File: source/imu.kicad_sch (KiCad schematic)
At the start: 5 parts

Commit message: Add files via upload
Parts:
- gave numbers to parts that had none: 5
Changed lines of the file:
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@@
   (symbol (lib_id "power:GND") (at 161.29 116.84 0) (unit 1)
     (in_bom yes) (on_board yes)
-    (property "Reference" "#PWR?" (id 0) (at 161.29 123.19 0)
+    (property "Reference" "#PWR0128" (id 0) (at 161.29 123.19 0)
       (effects (font (size 1.27 1.27)) hide)
     )
@@
   (symbol (lib_id "Cheap-FOCer-2-60mm-rescue:BMI160-IMU") (at 146.05 100.33 0) (unit 1)
     (in_bom yes) (on_board yes)
-    (property "Reference" "U?" (id 0) (at 146.05 78.3082 0))
+    (property "Reference" "U2" (id 0) (at 146.05 78.3082 0))
     (property "Value" "BMI160" (id 1) (at 146.05 80.6196 0))
     (property "Footprint" "Package_LGA:Bosch_LGA-14_3x2.5mm_P0.5mm" (id 2) (at 146.05 100.33 0)
@@
   (symbol (lib_id "power:GND") (at 124.46 101.6 0) (unit 1)
     (in_bom yes) (on_board yes)
-    (property "Reference" "#PWR?" (id 0) (at 124.46 107.95 0)
+    (property "Reference" "#PWR0125" (id 0) (at 124.46 107.95 0)
       (effects (font (size 1.27 1.27)) hide)
     )
@@
   (symbol (lib_id "power:VCC") (at 162.56 82.55 0) (unit 1)
     (in_bom yes) (on_board yes)
-    (property "Reference" "#PWR?" (id 0) (at 162.56 86.36 0)
+    (property "Reference" "#PWR0127" (id 0) (at 162.56 86.36 0)
       (effects (font (size 1.27 1.27)) hide)
     )
@@
   (symbol (lib_id "power:GND") (at 179.07 88.9 0) (unit 1)
     (in_bom yes) (on_board yes)
-    (property "Reference" "#PWR?" (id 0) (at 179.07 95.25 0)
+    (property "Reference" "#PWR0129" (id 0) (at 179.07 95.25 0)
       (effects (font (size 1.27 1.27)) hide)
     )
@@
   (symbol (lib_id "BLDC_4-rescue:C-RESCUE-BLDC_4") (at 170.18 82.55 270) (unit 1)
     (in_bom yes) (on_board yes)
-    (property "Reference" "C?" (id 0) (at 171.45 81.28 90)
+    (property "Reference" "C5" (id 0) (at 171.45 81.28 90)
       (effects (font (size 1.27 1.27)) (justify left))
     )
@@
   (symbol (lib_id "BLDC_4-rescue:R-RESCUE-BLDC_4") (at 121.92 86.36 180) (unit 1)
     (in_bom yes) (on_board yes)
-    (property "Reference" "R?" (id 0) (at 119.38 86.36 90))
+    (property "Reference" "R15" (id 0) (at 119.38 86.36 90))
     (property "Value" "1k" (id 1) (at 121.92 86.36 90))
     (property "Footprint" "Resistor_SMD:R_0603_1608Metric" (id 2) (at 121.92 86.36 0)
@@
   (symbol (lib_id "BLDC_4-rescue:R-RESCUE-BLDC_4") (at 113.03 86.36 0) (unit 1)
     (in_bom yes) (on_board yes)
-    (property "Reference" "R?" (id 0) (at 110.49 86.36 90))
+    (property "Reference" "R14" (id 0) (at 110.49 86.36 90))
     (property "Value" "1k" (id 1) (at 113.03 86.36 90))
     (property "Footprint" "Resistor_SMD:R_0603_1608Metric" (id 2) (at 113.03 86.36 0)
@@
   (symbol (lib_id "power:VCC") (at 121.92 76.2 0) (unit 1)
     (in_bom yes) (on_board yes)
-    (property "Reference" "#PWR?" (id 0) (at 121.92 80.01 0)
+    (property "Reference" "#PWR0126" (id 0) (at 121.92 80.01 0)
       (effects (font (size 1.27 1.27)) hide)
     )
@@
   (symbol (lib_id "BLDC_4-rescue:C-RESCUE-BLDC_4") (at 170.18 90.17 270) (unit 1)
     (in_bom yes) (on_board yes)
-    (property "Reference" "C?" (id 0) (at 171.45 91.44 90)
+    (property "Reference" "C6" (id 0) (at 171.45 91.44 90)
       (effects (font (size 1.27 1.27)) (justify left))
     )

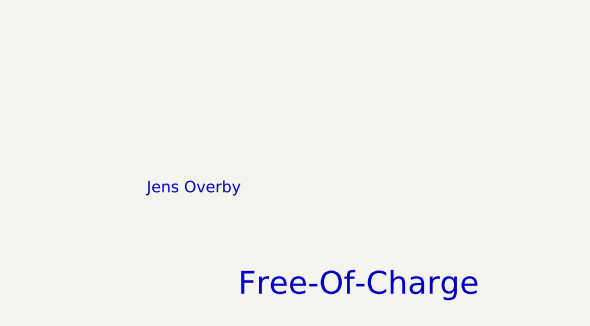
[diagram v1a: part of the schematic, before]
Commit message: Changes suggested by mxlemming, Elwin and hackey on Discord
New power supplies and using other op-amps for current sense
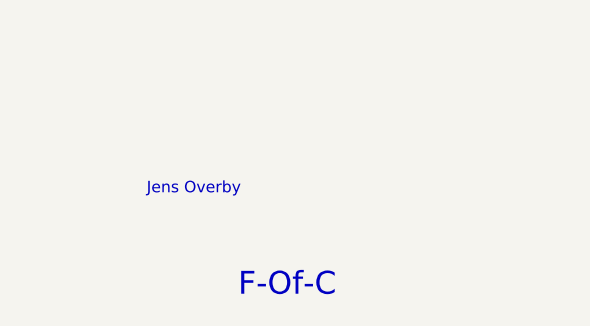
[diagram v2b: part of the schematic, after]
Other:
- note added: "F-Of-C"
- note removed: "Free-Of-Charge"
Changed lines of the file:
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@@
     (effects (font (size 1.27 1.27)) (justify left bottom))
   )
-  (text "Free-Of-Charge" (at 187.96 191.77 0)
+  (text "F-Of-C" (at 187.96 191.77 0)
     (effects (font (size 2.54 2.54)) (justify left bottom))
   )
